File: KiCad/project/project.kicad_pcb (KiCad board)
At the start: 4 copper layers, 40 x 40 mm, 19 parts, among them P1 Header-Female-2.54_1x3, U1 DRV8313PWPR

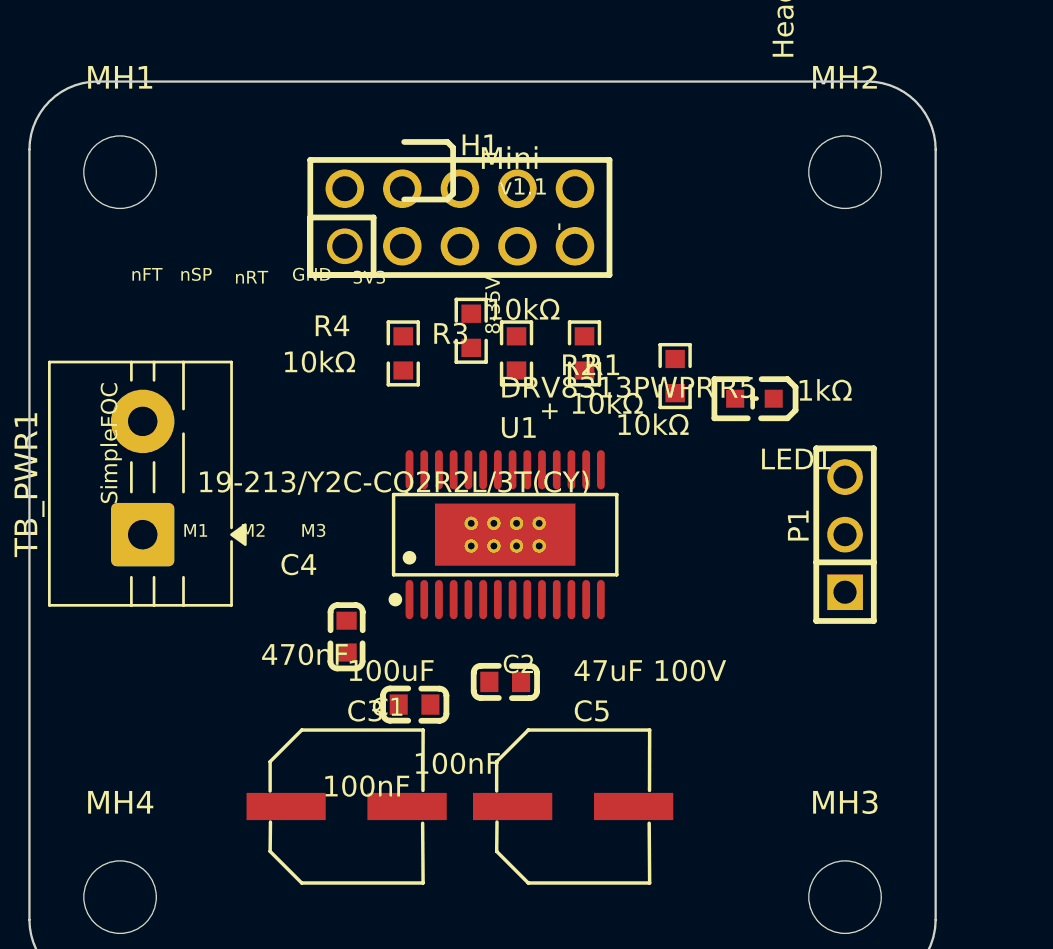
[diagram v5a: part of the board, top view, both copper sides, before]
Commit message: PCB: tool routing pass - signals on F/B.Cu + GND inner planes
route.py (F.Cu/B.Cu, 0.6mm power nets, neck-down): 17/17 single-ended +
15/17 multipoint routed. route_planes: solid GND planes on In1.Cu/In2.Cu,
24/24 GND pads stitched (10 new vias), 0.96mOhm / 13A. Zones filled.
DRC: 0 clearance, 0 shorts, 4 unconnected.

Pending hand-finish (HTSSOP 0.65mm escape, as predicted): EN pins 22/24,
VCC(VM) pins 4/11 + C2 - VCC better solved as a pour. Remaining DRC is
cosmetic silk (149) + the pre-existing U1 EP padstack artifact (10).

Co-Authored-By: Claude Opus 4.8 (1M context) <noreply@anthropic.com>
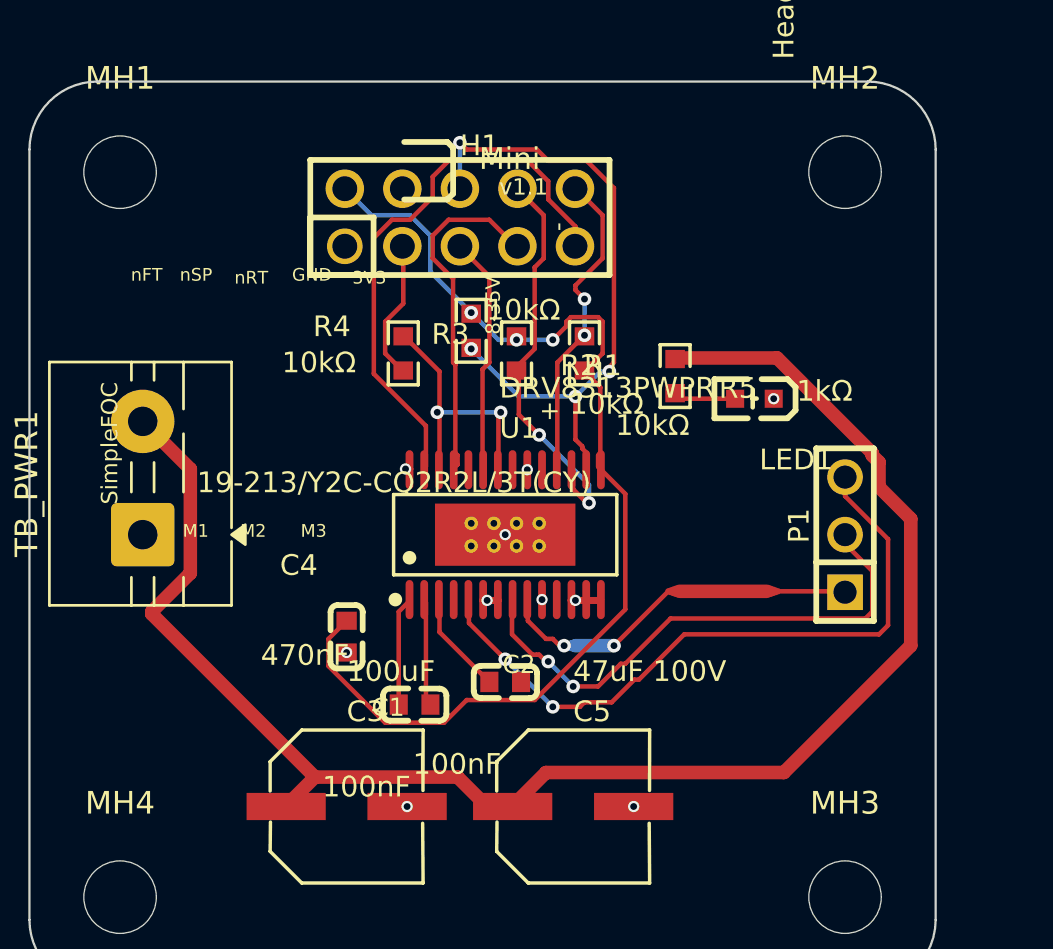
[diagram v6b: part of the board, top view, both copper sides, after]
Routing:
- net VCC: track 0.00 -> 71.7 mm
- net 3.3V: track 0.00 -> 48.6 mm, vias 0 -> 3
- net U1_5: track 0.00 -> 29.9 mm, vias 0 -> 2
- net NRES: track 0.00 -> 28.8 mm, vias 0 -> 4
- net IN1: track 0.00 -> 24.7 mm
- net U1_8: track 0.00 -> 23.7 mm, vias 0 -> 2
- net NSLP: track 0.00 -> 18.3 mm, vias 0 -> 2
- net U1_9: track 0.00 -> 16.4 mm, vias 0 -> 2
- net U1_25: track 0.00 -> 15.4 mm
- net NFLT: track 0.00 -> 14.2 mm, vias 0 -> 2
- net EN: track 0.00 -> 12.2 mm, vias 0 -> 2
- net IN3: track 0.00 -> 10.5 mm
- net R4_1: track 0.00 -> 6.26 mm
- net U1_1: track 0.00 -> 4.85 mm
- net U1_2: track 0.00 -> 4.77 mm
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- added copper zone on In1.Cu, net GND
- added copper zone on In2.Cu, net GND

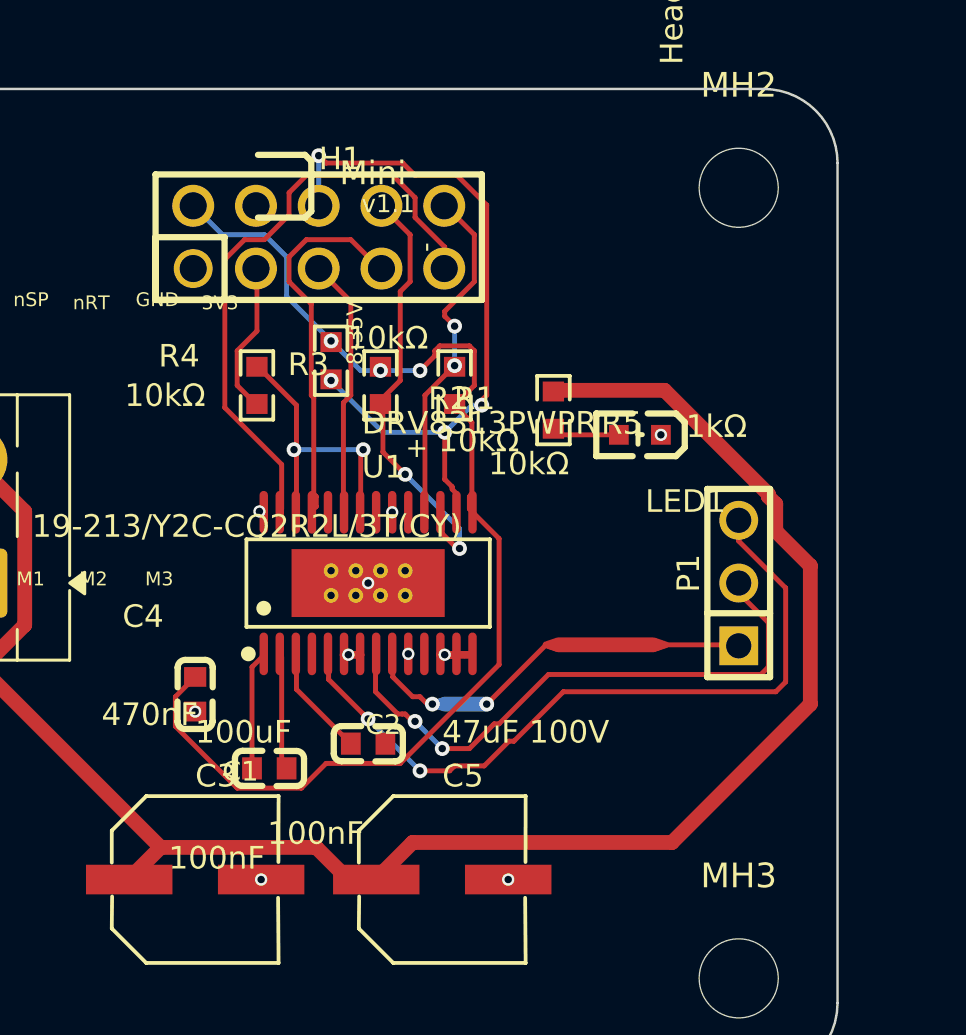
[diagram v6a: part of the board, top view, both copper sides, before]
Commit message: PCB: routing pass 2 - R5 sync fix, full signal/phase route, GND planes
- Fixed stale net: R5.1 VCC->3.3V (schematic has LED on V3P3OUT; PCB was
  never synced after the LED-resiting edit). Verified via full PCB<->sch
  connectivity diff - only other mismatch is U1 pin28 GND (PCB ties it,
  schematic floats it; recommend tying in schematic).
- route.py: all signals + all 3 phase outputs routed (F.Cu/B.Cu, 0.6mm
  power nets, neck-down). VCC routed first to claim its escape corridor.
- route_planes: GND planes In1/In2, 24/24 pads stitched. Zones filled.
- DRC: 0 shorts, 0 clearance. 3 unconnected: U1 VM pin 11 + two short
  escape stubs at the 0.65mm HTSSOP power row (fine-pitch escape, for GUI
  push-and-shove finish). Rest = cosmetic silk + U1 EP padstack artifact.

Co-Authored-By: Claude Opus 4.8 (1M context) <noreply@anthropic.com>
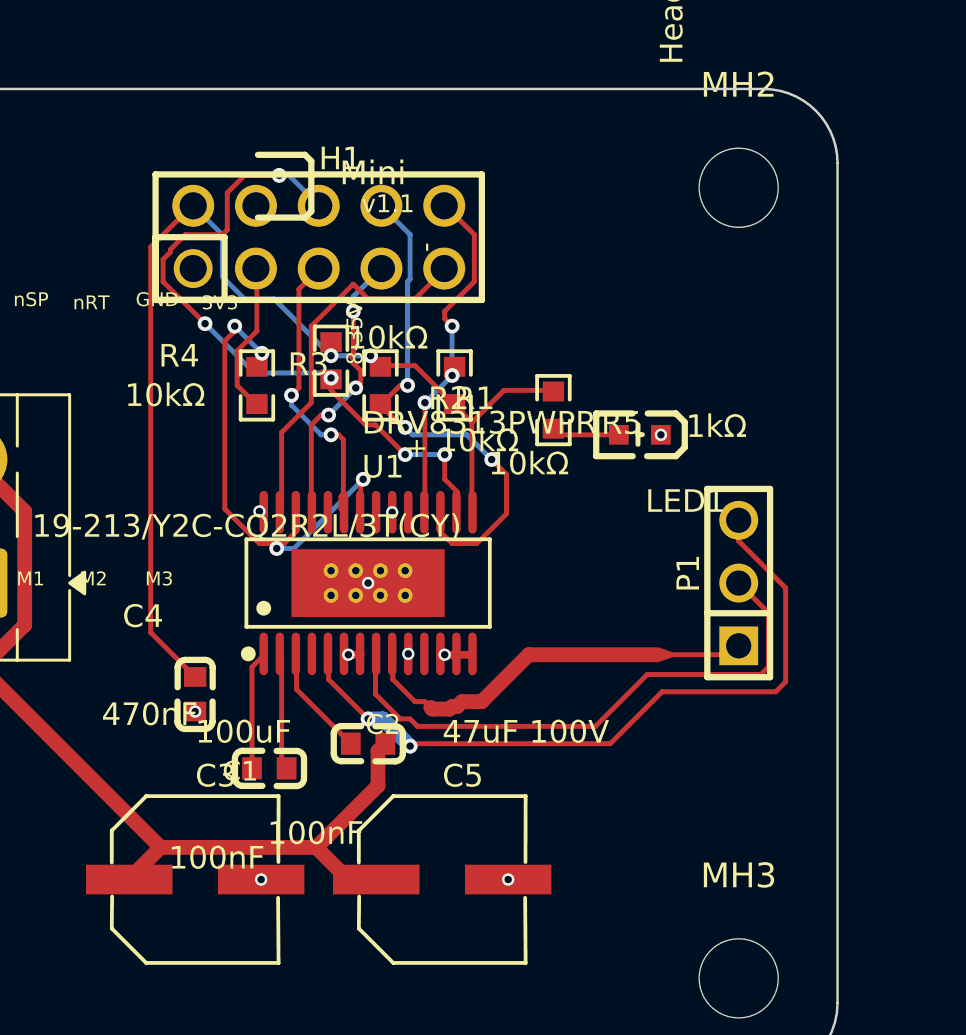
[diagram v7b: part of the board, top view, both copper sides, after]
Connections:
- R5 pad 1: VCC -> 3.3V
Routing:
- net VCC: track 71.7 -> 36.8 mm
- net IN1: track 24.7 -> 15.0 mm
- net EN: track 12.2 -> 20.5 mm, vias 2 -> 4
- net U1_25: track 15.4 -> 11.6 mm, vias 0 -> 3
- net 3.3V: track 48.6 -> 44.8 mm, vias 3 -> 2
- net NSLP: track 18.3 -> 21.5 mm, vias 2 -> 3
- net NRES: track 28.8 -> 27.3 mm, vias 4 -> 5
- net IN3: track 10.5 -> 11.7 mm, vias 0 -> 2
- net U1_5: track 29.9 -> 29.1 mm
- net U1_8: track 23.7 -> 23.0 mm, vias 2 -> 0
- net NFLT: track 14.2 -> 14.5 mm, vias 2 -> 3
- net U1_9: track 16.4 -> 16.7 mm, vias 2 -> 0

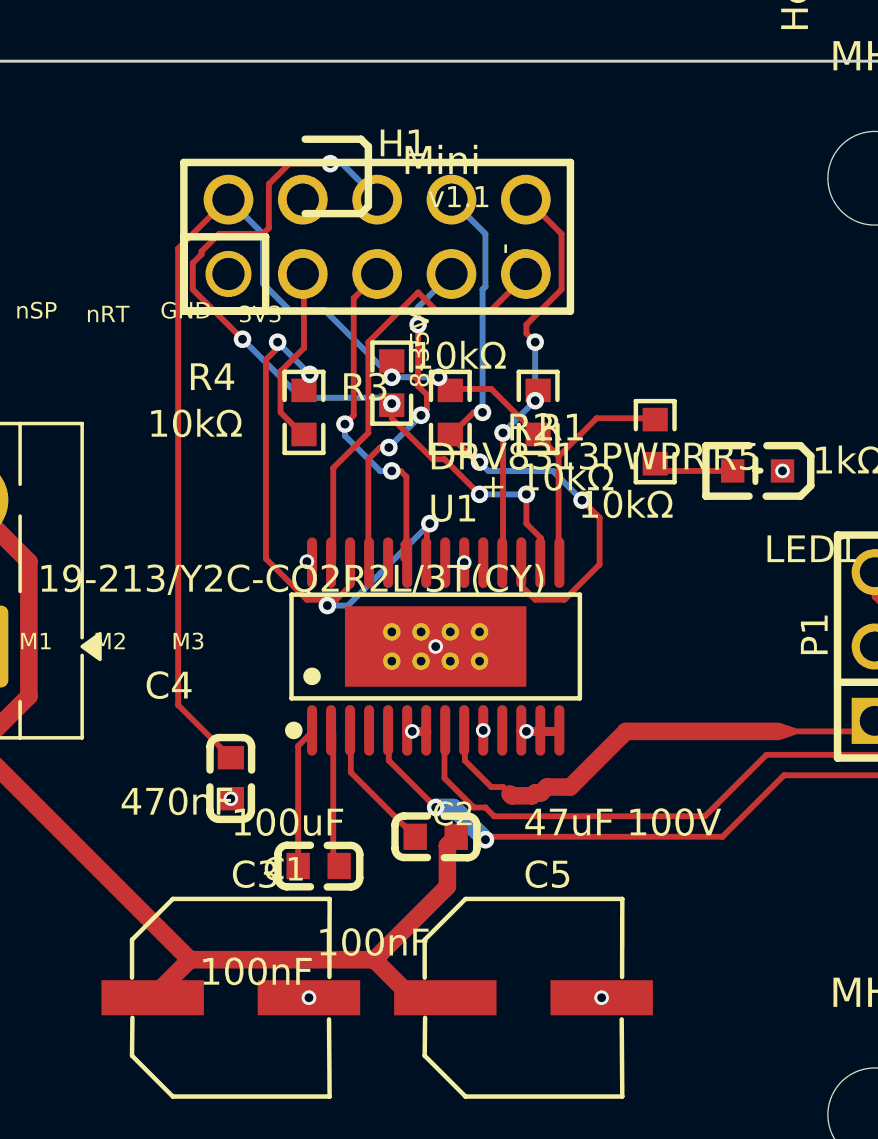
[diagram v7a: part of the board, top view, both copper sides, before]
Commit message: PCB: hand-route both VM pins (4 & 11) + silk to 60V rev
Connected U1 VM pins 4 and 11 to the VCC rail with B.Cu via-jogs threaded
clear of the phase escapes (U1_5/U1_9) and the VCP trace (U1_3 kinks right
at y114.3, so pin 4 drops above it). VCC now FULLY CONNECTED; 0 shorts,
0 clearance. Silk: 8-35V -> 8-60V, v1.1 -> v2.0.

Remaining: 1 EN ratsnest near-miss from the autoroute (check_connected
counts EN fully connected; KiCad flags a hairline gap) - trivial GUI snap.

Co-Authored-By: Claude Opus 4.8 (1M context) <noreply@anthropic.com>
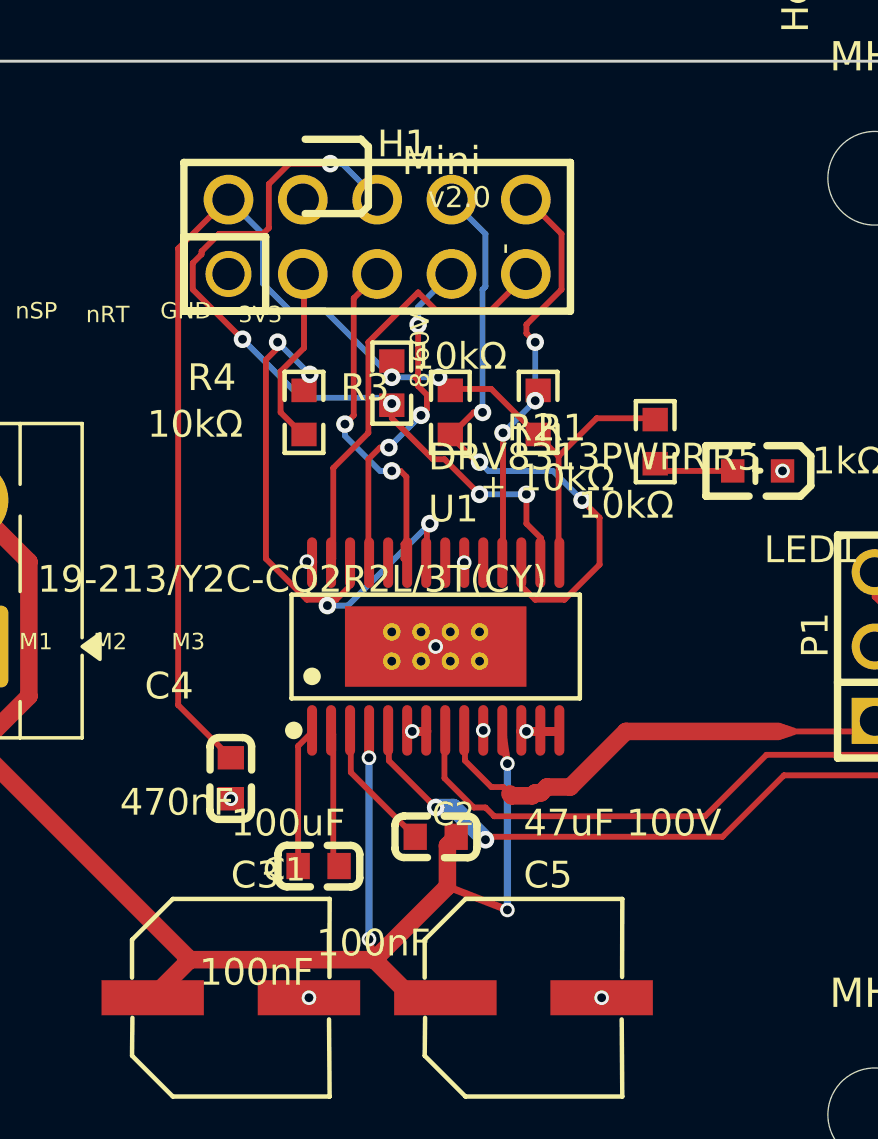
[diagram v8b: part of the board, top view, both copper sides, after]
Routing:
- net VCC: track 36.8 -> 52.9 mm, vias 0 -> 4
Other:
- board text added: "8-60V"
- board text added: "Mini v2.0"
- board text added: "v2.0"
- board text removed: "8-35V"
- board text removed: "Mini v1.1"
- board text removed: "v1.1"
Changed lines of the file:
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@@
 		)
 	)
-	(gr_text "8-35V"
+	(gr_text "8-60V"
 		(at 154.092 101.176 90)
 		(layer "F.SilkS")
@@
 		)
 	)
-	(gr_text "v1.1"
+	(gr_text "v2.0"
 		(at 154.732 94.233 0)
 		(layer "F.SilkS")
@@
 		)
 	)
-	(gr_text "Mini v1.1"
+	(gr_text "Mini v2.0"
 		(at 156.129 109.266 0)
 		(layer "B.SilkS")
@@
 		)
 	)
-	(gr_text "8-35V"
+	(gr_text "8-60V"
 		(at 153.805 97.62 90)
 		(layer "B.SilkS")
@@
 	)
 	(segment
+		(start 157.45 119)
+		(end 155.4 118.2)
+		(width 0.25)
+		(layer "F.Cu")
+		(net "VCC")
+	)
+	(segment
+		(start 152.72 120)
+		(end 152.9 120.7)
+		(width 0.25)
+		(layer "F.Cu")
+		(net "VCC")
+	)
+	(segment
 		(start 141.1 111.7)
 		(end 141.1 107.1)
@@
 	)
 	(segment
+		(start 152.72 112.87)
+		(end 152.72 113.8)
+		(width 0.25)
+		(layer "F.Cu")
+		(net "VCC")
+	)
+	(segment
 		(start 141.1 107.1)
 		(end 139 105)
@@
 		(net "VCC")
 	)
+	(segment
+		(start 157.28 112.87)
+		(end 157.45 114)
+		(width 0.25)
+		(layer "F.Cu")
+		(net "VCC")
+	)
+	(via
+		(at 157.45 119)
+		(size 0.5)
+		(drill 0.3)
+		(layers "F.Cu" "B.Cu")
+		(net "VCC")
+	)
+	(via
+		(at 152.72 120)
+		(size 0.5)
+		(drill 0.3)
+		(layers "F.Cu" "B.Cu")
+		(net "VCC")
+	)
+	(via
+		(at 152.72 113.8)
+		(size 0.5)
+		(drill 0.3)
+		(layers "F.Cu" "B.Cu")
+		(net "VCC")
+	)
+	(via
+		(at 157.45 114)
+		(size 0.5)
+		(drill 0.3)
+		(layers "F.Cu" "B.Cu")
+		(net "VCC")
+	)
+	(segment
+		(start 157.45 114)
+		(end 157.45 119)
+		(width 0.25)
+		(layer "B.Cu")
+		(net "VCC")
+	)
+	(segment
+		(start 152.72 113.8)
+		(end 152.72 120)
+		(width 0.25)
+		(layer "B.Cu")
+		(net "VCC")
+	)
